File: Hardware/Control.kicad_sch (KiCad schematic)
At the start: 42 parts, among them J1 XKTF-015-N, SW1 PTS_647_SN50_SMTR2_LFS, SW2 PTS_647_SN50_SMTR2_LFS, SW3 PTS_647_SN50_SMTR2_LFS, U1 RP2354B, X2 ABM8-272-T3

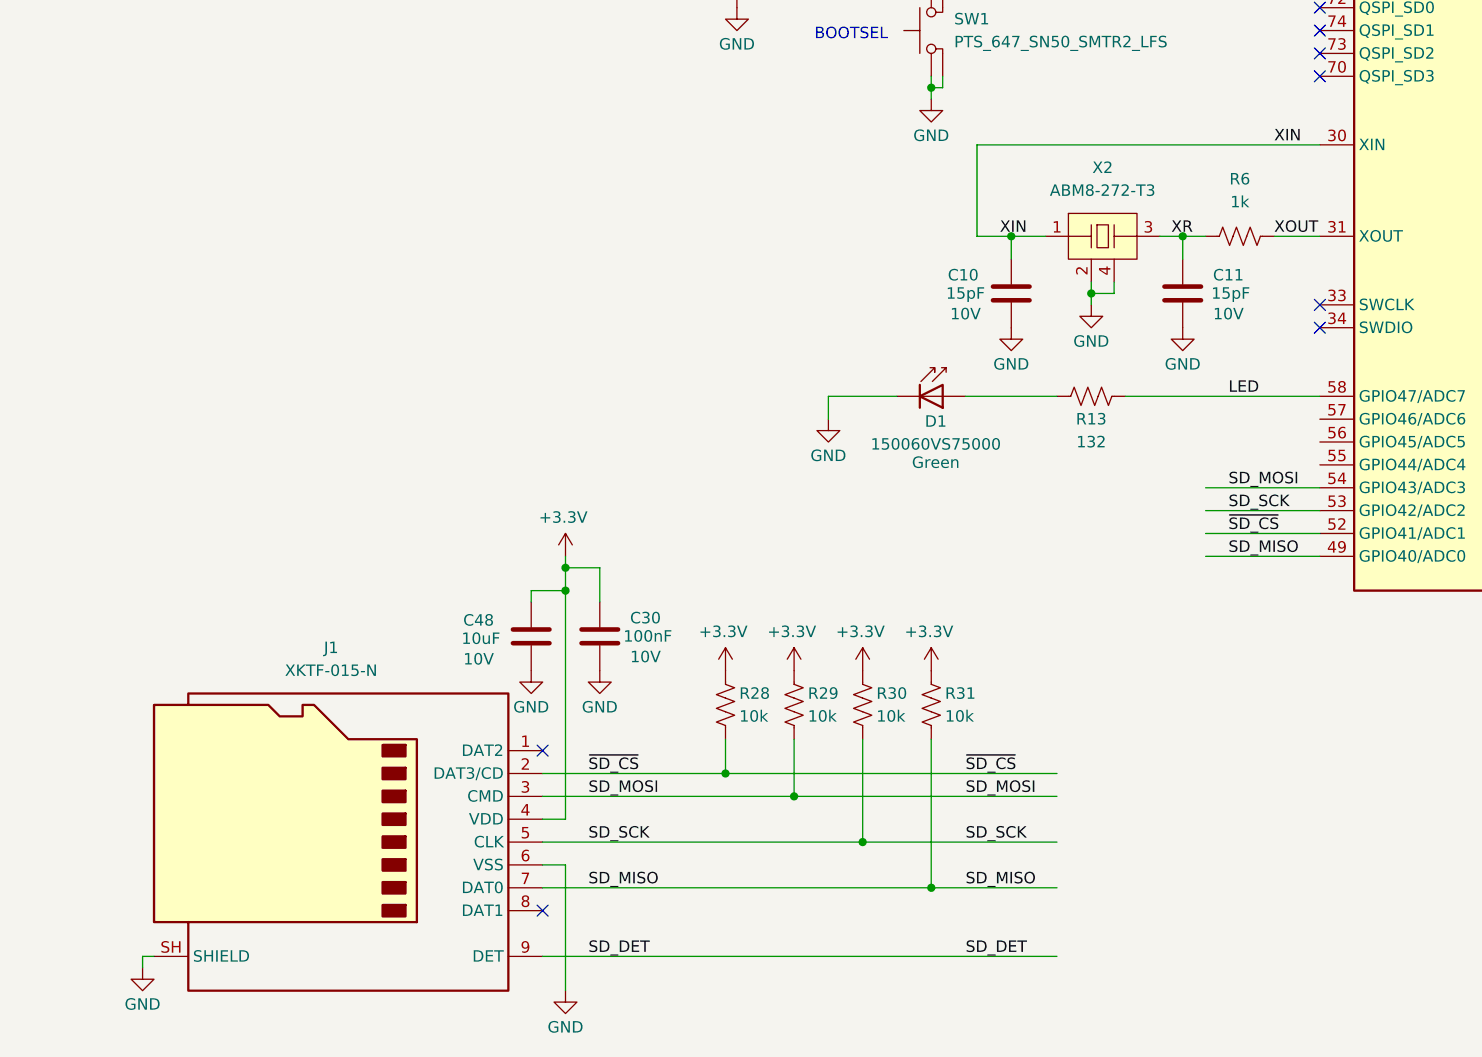
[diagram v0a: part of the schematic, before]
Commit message: speaker output
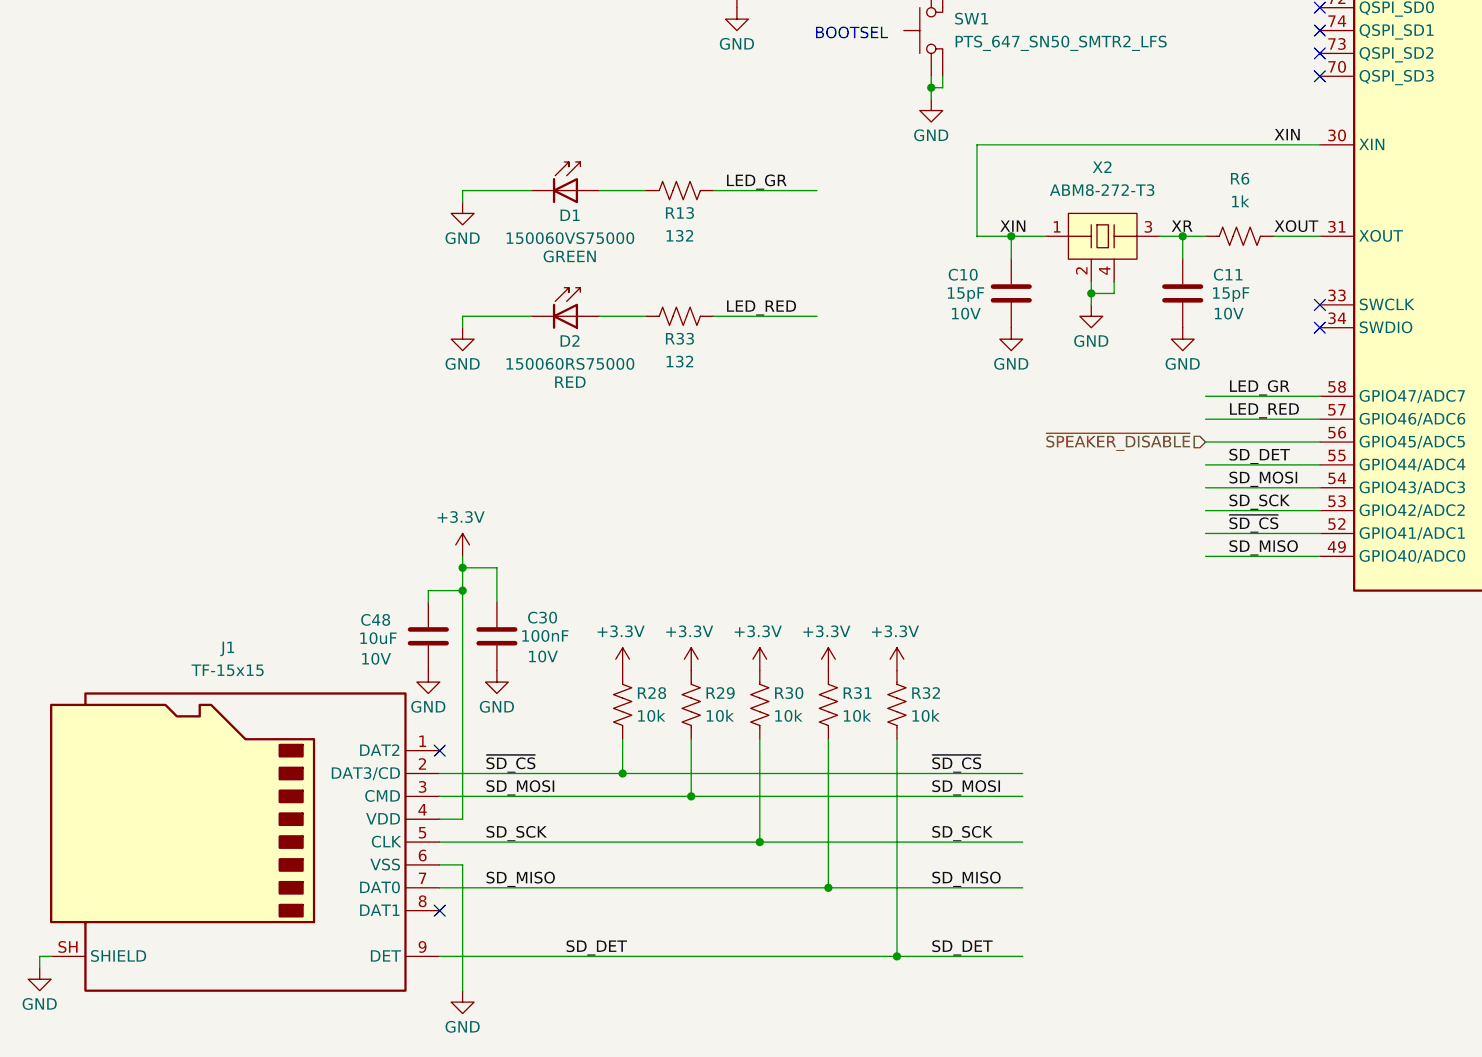
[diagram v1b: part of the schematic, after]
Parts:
- added D2: 150060RS75000, symbol LED:CQY99
- added R32: 10k, symbol Device:R_US
- added R33: 132, symbol Device:R_US
- D1: Color Green -> GREEN
- J1: value XKTF-015-N -> TF-15x15
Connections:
- net +3.3V: now also R32.2
- net GND: now also D2.1 (K)
- net SD_DET: now also U1.55 (GPIO44/ADC4), R32.1
- net ~{SPEAKER_DISABLE}: now reaches U1.56 (GPIO45/ADC5)
- net LED_RED: now reaches U1.57 (GPIO46/ADC6)
- net LED_RED: now also R33.1
- net LED renamed LED_GR
- new net: D2.2 (A), R33.2
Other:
- moved on the sheet: C30, C48, J1, R28, R29, R30, R31

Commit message: footprint assignment
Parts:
- C10, C11: footprint (none) -> Capacitor_SMD:C_0402_1005Metric; MPN (none) -> CC0402JRNPO9BN150
- C12, C13, C14, C15: footprint (none) -> Capacitor_SMD:C_0402_1005Metric; MPN (none) -> CL05A475MP5NRNC
- C16, C17, C18, C19, C20, C21, C22, C23, C24, C25, C26, C27, C28, C29, C30: footprint (none) -> Capacitor_SMD:C_0402_1005Metric; MPN (none) -> GRM155R71A104KA01D
- C48: footprint (none) -> Capacitor_SMD:C_0402_1005Metric; MPN (none) -> CL05A106MQ5NUNC
- D1: footprint (none) -> LED_SMD:LED_0603_1608Metric; MPN (none) -> 150060VS75000
- D2: footprint (none) -> LED_SMD:LED_0603_1608Metric; MPN (none) -> 150060RS75000
- J1: value TF-15x15 -> DM3AT-SF-PEJM5; footprint (none) -> Connector_Card:microSD_HC_Hirose_DM3AT-SF-PEJM5; MPN (none) -> DM3AT-SF-PEJM5
- L1: footprint (none) -> Inductor_SMD:L_0805_2012Metric; MPN (none) -> AOTA-B201610S3R3-101-T
- SW1, SW2, SW3: footprint (none) -> Button_Switch_SMD:SW_SPST_PTS647_Sx50; MPN (none) -> PTS_647_SN50_SMTR2_LFS
- U1: MPN (none) -> RP2354B
- X2: footprint (none) -> Crystal:Crystal_SMD_Abracon_ABM8G-4Pin_3.2x2.5mm; MPN (none) -> ABM8-272-T3
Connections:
- net +3.3V: now also J1.9 (DET_A); no longer R32.2
- net GND: now also R32.1
- net SD_DET: now also J1.10 (DET_B), R32.2; no longer J1.9 (DET), R32.1

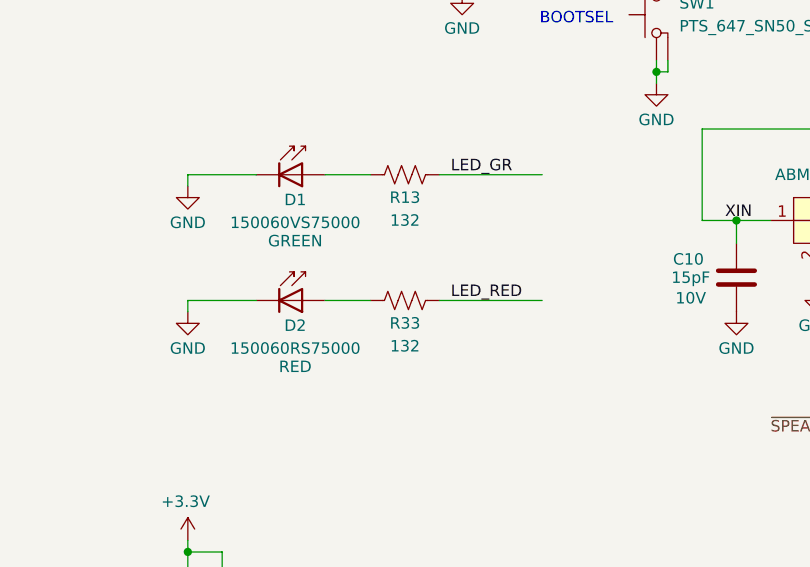
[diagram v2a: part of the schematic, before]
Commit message: link footprints to symbols
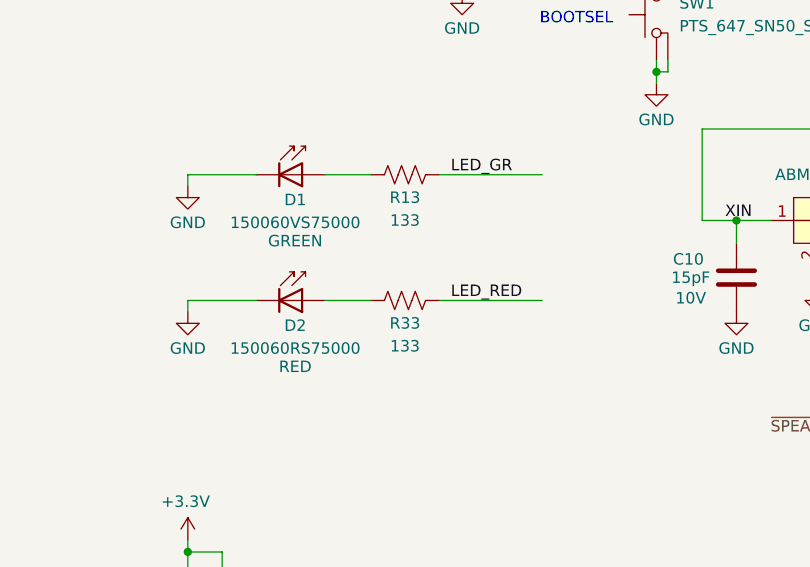
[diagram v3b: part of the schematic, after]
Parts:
- R10, R11, R6, R7: footprint (none) -> Resistor_SMD:R_0402_1005Metric; MPN (none) -> RC0402JR-071KL
- R12, R28, R29, R30, R31, R32: footprint (none) -> Resistor_SMD:R_0402_1005Metric; MPN (none) -> RC0402FR-0710KL
- R13, R33: value 132 -> 133; footprint (none) -> Resistor_SMD:R_0402_1005Metric; MPN (none) -> RC0402FR-07133RL
- R8, R9: footprint (none) -> Resistor_SMD:R_0402_1005Metric; MPN (none) -> RC0402FR-0727RL
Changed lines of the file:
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@@
 			)
 		)
-		(property "Footprint" ""
+		(property "Footprint" "Resistor_SMD:R_0402_1005Metric"
 			(at 124.714 200.406 90)
 			(hide yes)
@@
 			)
 		)
-		(property "Datasheet" ""
+		(property "Datasheet" "https://yageogroup.com/content/datasheet/asset/file/PYU-RC_GROUP_51_ROHS_L"
 			(at 125.73 200.66 0)
 			(hide yes)
@@
 			)
 		)
+		(property "MPN" "RC0402FR-0710KL"
+			(at 125.73 200.66 0)
+			(hide yes)
+			(show_name no)
+			(do_not_autoplace no)
+			(effects
+				(font
+					(size 1.27 1.27)
+				)
+			)
+		)
 		(pin "1"
 		)
@@
 			)
 		)
-		(property "Footprint" ""
+		(property "Footprint" "Resistor_SMD:R_0402_1005Metric"
 			(at 155.956 73.406 90)
 			(hide yes)
@@
 			)
 		)
-		(property "Datasheet" ""
+		(property "Datasheet" "https://yageogroup.com/content/datasheet/asset/file/PYU-RC_GROUP_51_ROHS_L"
 			(at 156.21 72.39 0)
 			(hide yes)
@@
 			)
 		)
+		(property "MPN" "RC0402JR-071KL"
+			(at 156.21 72.39 90)
+			(hide yes)
+			(show_name no)
+			(do_not_autoplace no)
+			(effects
+				(font
+					(size 1.27 1.27)
+				)
+			)
+		)
 		(pin "1"
 		)
@@
 			)
 		)
-		(property "Footprint" ""
+		(property "Footprint" "Resistor_SMD:R_0402_1005Metric"
 			(at 270.256 190.754 90)
 			(hide yes)
@@
 			)
 		)
-		(property "Datasheet" ""
+		(property "Datasheet" "https://yageogroup.com/content/datasheet/asset/file/PYU-RC_GROUP_51_ROHS_L"
 			(at 269.24 190.5 0)
 			(hide yes)
@@
 			)
 		)
+		(property "MPN" "RC0402FR-0710KL"
+			(at 269.24 190.5 0)
+			(hide yes)
+			(show_name no)
+			(do_not_autoplace no)
+			(effects
+				(font
+					(size 1.27 1.27)
+				)
+			)
+		)
 		(pin "1"
 		)
@@
 			)
 		)
-		(property "Footprint" ""
+		(property "Footprint" "Resistor_SMD:R_0402_1005Metric"
 			(at 132.334 200.406 90)
 			(hide yes)
@@
 			)
 		)
-		(property "Datasheet" ""
+		(property "Datasheet" "https://yageogroup.com/content/datasheet/asset/file/PYU-RC_GROUP_51_ROHS_L"
 			(at 133.35 200.66 0)
 			(hide yes)
@@
 			)
 		)
+		(property "MPN" "RC0402FR-0710KL"
+			(at 133.35 200.66 0)
+			(hide yes)
+			(show_name no)
+			(do_not_autoplace no)
+			(effects
+				(font
+					(size 1.27 1.27)
+				)
+			)
+		)
 		(pin "1"
 		)
@@
 			)
 		)
-		(property "Footprint" ""
+		(property "Footprint" "Resistor_SMD:R_0402_1005Metric"
 			(at 181.356 111.506 90)
 			(hide yes)
@@
 			)
 		)
-		(property "Datasheet" ""
+		(property "Datasheet" "https://yageogroup.com/content/datasheet/asset/file/PYU-RC_GROUP_51_ROHS_L"
 			(at 181.61 110.49 0)
 			(hide yes)
@@
 			)
 		)
+		(property "MPN" "RC0402FR-0727RL"
+			(at 181.61 110.49 90)
+			(hide yes)
+			(show_name no)
+			(do_not_autoplace no)
+			(effects
+				(font
+					(size 1.27 1.27)
+				)
+			)
+		)
 		(pin "1"
 		)
@@
 			)
 		)
-		(property "Footprint" ""
+		(property "Footprint" "Resistor_SMD:R_0402_1005Metric"
 			(at 167.386 119.126 90)
 			(hide yes)
@@
 			)
 		)
-		(property "Datasheet" ""
+		(property "Datasheet" "https://yageogroup.com/content/datasheet/asset/file/PYU-RC_GROUP_51_ROHS_L"
 			(at 167.64 118.11 0)
 			(hide yes)
@@
 			)
 		)
+		(property "MPN" "RC0402JR-071KL"
+			(at 167.64 118.11 90)
+			(hide yes)
+			(show_name no)
+			(do_not_autoplace no)
+			(effects
+				(font
+					(size 1.27 1.27)
+				)
+			)
+		)
 		(pin "1"
 		)
@@
 			)
 		)
-		(property "Footprint" ""
+		(property "Footprint" "Resistor_SMD:R_0402_1005Metric"
 			(at 109.474 237.236 90)
 			(hide yes)
@@
 			)
 		)
-		(property "Datasheet" ""
+		(property "Datasheet" "https://yageogroup.com/content/datasheet/asset/file/PYU-RC_GROUP_51_ROHS_L"
 			(at 110.49 237.49 0)
 			(hide yes)
@@
 			)
 		)
+		(property "MPN" "RC0402FR-0710KL"
+			(at 110.49 237.49 0)
+			(hide yes)
+			(show_name no)
+			(do_not_autoplace no)
+			(effects
+				(font
+					(size 1.27 1.27)
+				)
+			)
+		)
 		(pin "1"
 		)
@@
 			)
 		)
-		(property "Value" "132"
+		(property "Value" "133"
 			(at 116.84 162.56 90)
 			(show_name no)
@@
 			)
 		)
-		(property "Footprint" ""
+		(property "Footprint" "Resistor_SMD:R_0402_1005Metric"
 			(at 116.586 158.496 90)
 			(hide yes)
@@
 			)
 		)
-		(property "Datasheet" ""
+		(property "Datasheet" "https://yageogroup.com/content/datasheet/asset/file/PYU-RC_GROUP_51_ROHS_L"
 			(at 116.84 157.48 0)
 			(hide yes)
@@
 			)
 		)
+		(property "MPN" "RC0402FR-07133RL"
+			(at 116.84 157.48 90)
+			(hide yes)
+			(show_name no)
+			(do_not_autoplace no)
+			(effects
+				(font
+					(size 1.27 1.27)
+				)
+			)
+		)
 		(pin "1"
 		)
@@
 			)
 		)
-		(property "Footprint" ""
+		(property "Footprint" "Resistor_SMD:R_0402_1005Metric"
 			(at 181.356 108.966 90)
 			(hide yes)
@@
 			)
 		)
-		(property "Datasheet" ""
+		(property "Datasheet" "https://yageogroup.com/content/datasheet/asset/file/PYU-RC_GROUP_51_ROHS_L"
 			(at 181.61 107.95 0)
 			(hide yes)
@@
 			)
 		)
+		(property "MPN" "RC0402FR-0727RL"
+			(at 181.61 107.95 90)
+			(hide yes)
+			(show_name no)
+			(do_not_autoplace no)
+			(effects
+				(font
+					(size 1.27 1.27)
+				)
+			)
+		)
 		(pin "1"
 		)
@@
 			)
 		)
-		(property "Footprint" ""
+		(property "Footprint" "Resistor_SMD:R_0402_1005Metric"
 			(at 122.174 119.126 90)
 			(hide yes)
@@
 			)
 		)
-		(property "Datasheet" ""
+		(property "Datasheet" "https://yageogroup.com/content/datasheet/asset/file/PYU-RC_GROUP_51_ROHS_L"
 			(at 123.19 119.38 0)
 			(hide yes)
@@
 			)
 		)
+		(property "MPN" "RC0402JR-071KL"
+			(at 123.19 119.38 0)
+			(hide yes)
+			(show_name no)
+			(do_not_autoplace no)
+			(effects
+				(font
+					(size 1.27 1.27)
+				)
+			)
+		)
 		(pin "1"
 		)
@@
 			)
 		)
-		(property "Value" "132"
+		(property "Value" "133"
 			(at 116.84 148.59 90)
 			(show_name no)
@@
 			)
 		)
-		(property "Footprint" ""
+		(property "Footprint" "Resistor_SMD:R_0402_1005Metric"
 			(at 116.586 144.526 90)
 			(hide yes)
@@
 			)
 		)
-		(property "Datasheet" ""
+		(property "Datasheet" "https://yageogroup.com/content/datasheet/asset/file/PYU-RC_GROUP_51_ROHS_L"
 			(at 116.84 143.51 0)
 			(hide yes)
@@
 			)
 		)
+		(property "MPN" "RC0402FR-07133RL"
+			(at 116.84 143.51 90)
+			(hide yes)
+			(show_name no)
+			(do_not_autoplace no)
+			(effects
+				(font
+					(size 1.27 1.27)
+				)
+			)
+		)
 		(pin "1"
 		)
@@
 			)
 		)
-		(property "Footprint" ""
+		(property "Footprint" "Resistor_SMD:R_0402_1005Metric"
 			(at 117.094 200.406 90)
 			(hide yes)
@@
 			)
 		)
-		(property "Datasheet" ""
+		(property "Datasheet" "https://yageogroup.com/content/datasheet/asset/file/PYU-RC_GROUP_51_ROHS_L"
 			(at 118.11 200.66 0)
 			(hide yes)
@@
 			)
 		)
+		(property "MPN" "RC0402FR-0710KL"
+			(at 118.11 200.66 0)
+			(hide yes)
+			(show_name no)
+			(do_not_autoplace no)
+			(effects
+				(font
+					(size 1.27 1.27)
+				)
+			)
+		)
 		(pin "1"
 		)
@@
 			)
 		)
-		(property "Footprint" ""
+		(property "Footprint" "Resistor_SMD:R_0402_1005Metric"
 			(at 178.816 149.606 90)
 			(hide yes)
@@
 			)
 		)
-		(property "Datasheet" ""
+		(property "Datasheet" "https://yageogroup.com/content/datasheet/asset/file/PYU-RC_GROUP_51_ROHS_L"
 			(at 179.07 148.59 0)
 			(hide yes)
@@
 			)
 		)
+		(property "MPN" "RC0402JR-071KL"
+			(at 179.07 148.59 90)
+			(hide yes)
+			(show_name no)
+			(do_not_autoplace no)
+			(effects
+				(font
+					(size 1.27 1.27)
+				)
+			)
+		)
 		(pin "1"
 		)
@@
 			)
 		)
-		(property "Footprint" ""
+		(property "Footprint" "Resistor_SMD:R_0402_1005Metric"
 			(at 109.474 200.406 90)
 			(hide yes)
@@
 			)
 		)
-		(property "Datasheet" ""
+		(property "Datasheet" "https://yageogroup.com/content/datasheet/asset/file/PYU-RC_GROUP_51_ROHS_L"
 			(at 110.49 200.66 0)
 			(hide yes)
@@
 			(at 110.49 200.66 0)
 			(hide yes)
+			(show_name no)
+			(do_not_autoplace no)
+			(effects
+				(font
+					(size 1.27 1.27)
+				)
+			)
+		)
+		(property "MPN" "RC0402FR-0710KL"
+			(at 110.49 200.66 0)
+			(hide yes)
